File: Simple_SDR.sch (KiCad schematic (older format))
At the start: 0 parts

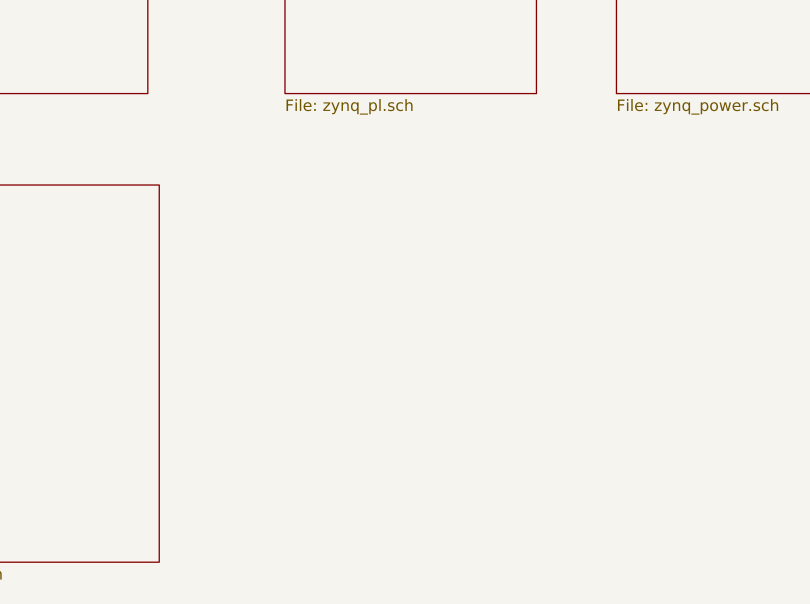
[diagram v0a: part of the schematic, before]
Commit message: Add regulator page and rework its symbol footprint
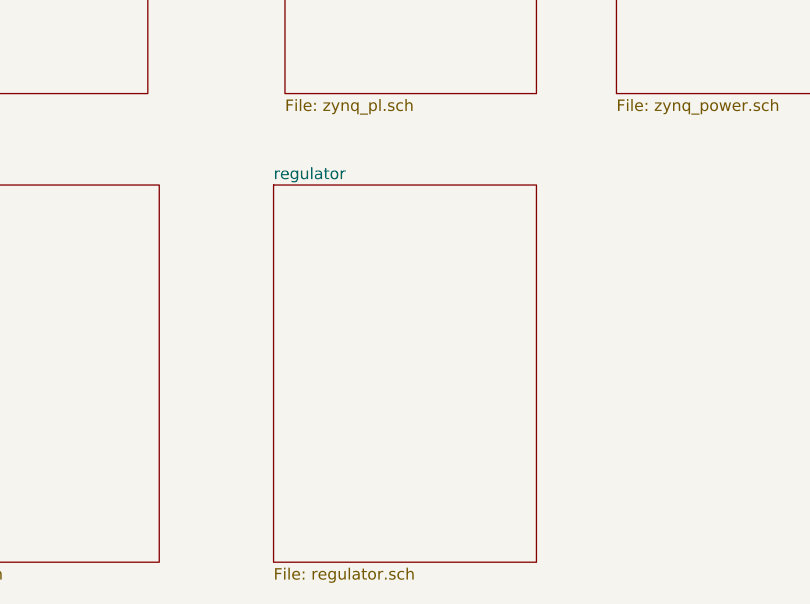
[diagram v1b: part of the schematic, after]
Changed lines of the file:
@@
 $Descr A4 11693 8268
 encoding utf-8
-Sheet 1 6
+Sheet 1 7
 Title ""
 Date ""
@@
 F1 "zynq_ddr.sch" 50
 $EndSheet
+$Sheet
+S 3300 3900 1150 1650
+U 675F00E9
+F0 "regulator" 50
+F1 "regulator.sch" 50
+$EndSheet
 $EndSCHEMATC

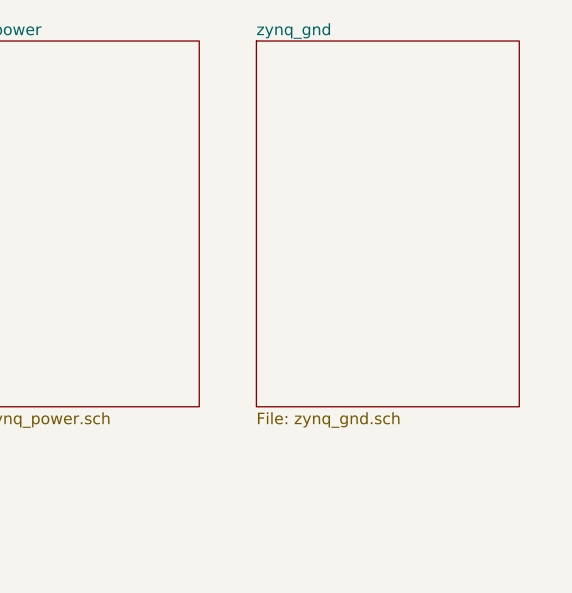
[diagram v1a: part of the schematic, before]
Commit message: Update schematic sheets
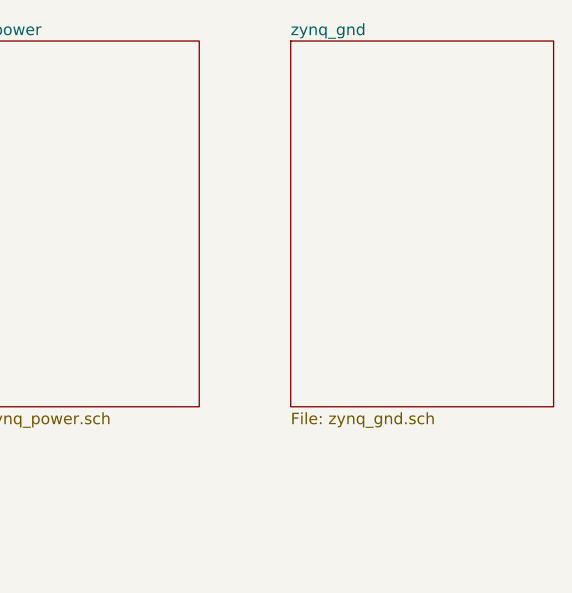
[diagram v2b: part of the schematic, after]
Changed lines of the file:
@@
-$EndSheet
-$Sheet
-S 6150 1900 1150 1600
-U 675D4290
-F0 "zynq_gnd" 50
-F1 "zynq_gnd.sch" 50
 $EndSheet
 $Sheet
@@
 F1 "regulator.sch" 50
 $EndSheet
+$Sheet
+S 6300 1900 1150 1600
+U 675F31B2
+F0 "zynq_gnd" 50
+F1 "zynq_gnd.sch" 50
+$EndSheet
 $EndSCHEMATC

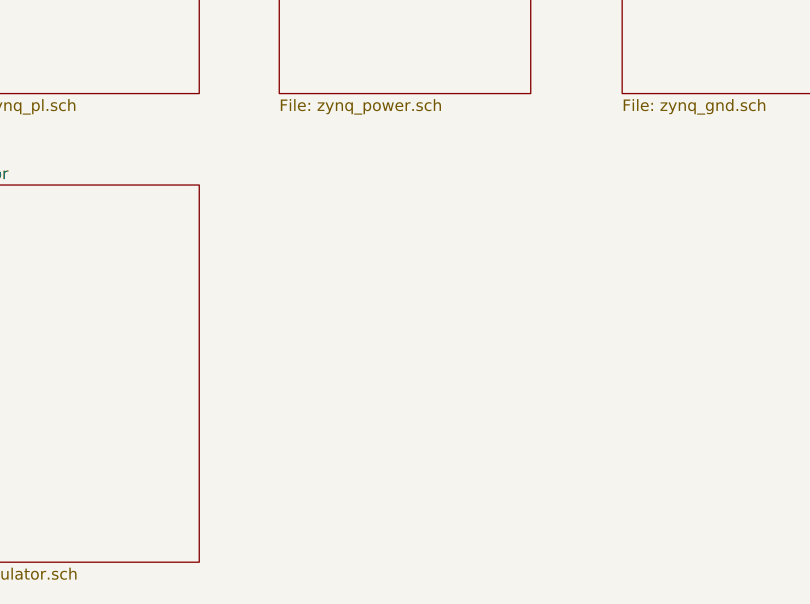
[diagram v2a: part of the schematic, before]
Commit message: Create new sheet for DDR3L schematic
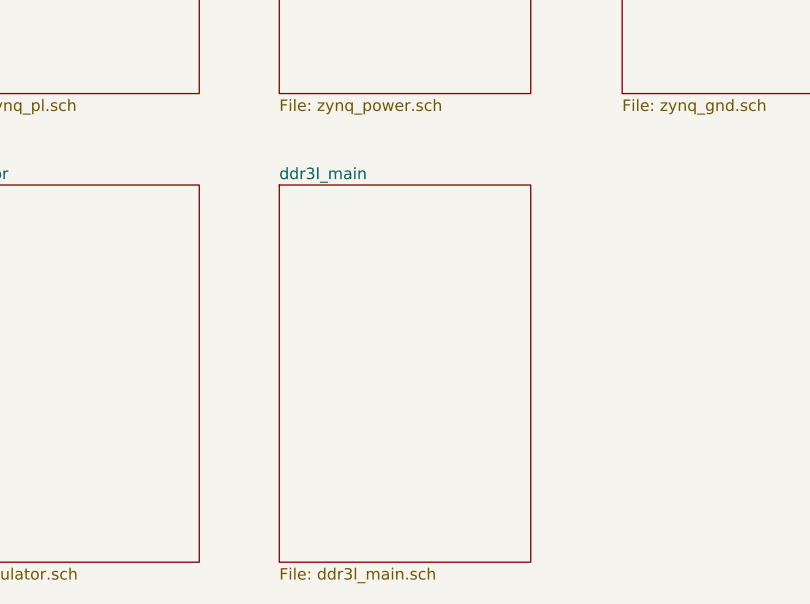
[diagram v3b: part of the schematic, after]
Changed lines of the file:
@@
 $Descr A4 11693 8268
 encoding utf-8
-Sheet 1 7
+Sheet 1 8
 Title ""
 Date ""
@@
 F1 "zynq_gnd.sch" 50
 $EndSheet
+$Sheet
+S 4800 3900 1100 1650
+U 675F7864
+F0 "ddr3l_main" 50
+F1 "ddr3l_main.sch" 50
+$EndSheet
 $EndSCHEMATC
